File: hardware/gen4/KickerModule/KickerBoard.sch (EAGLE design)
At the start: 110 parts

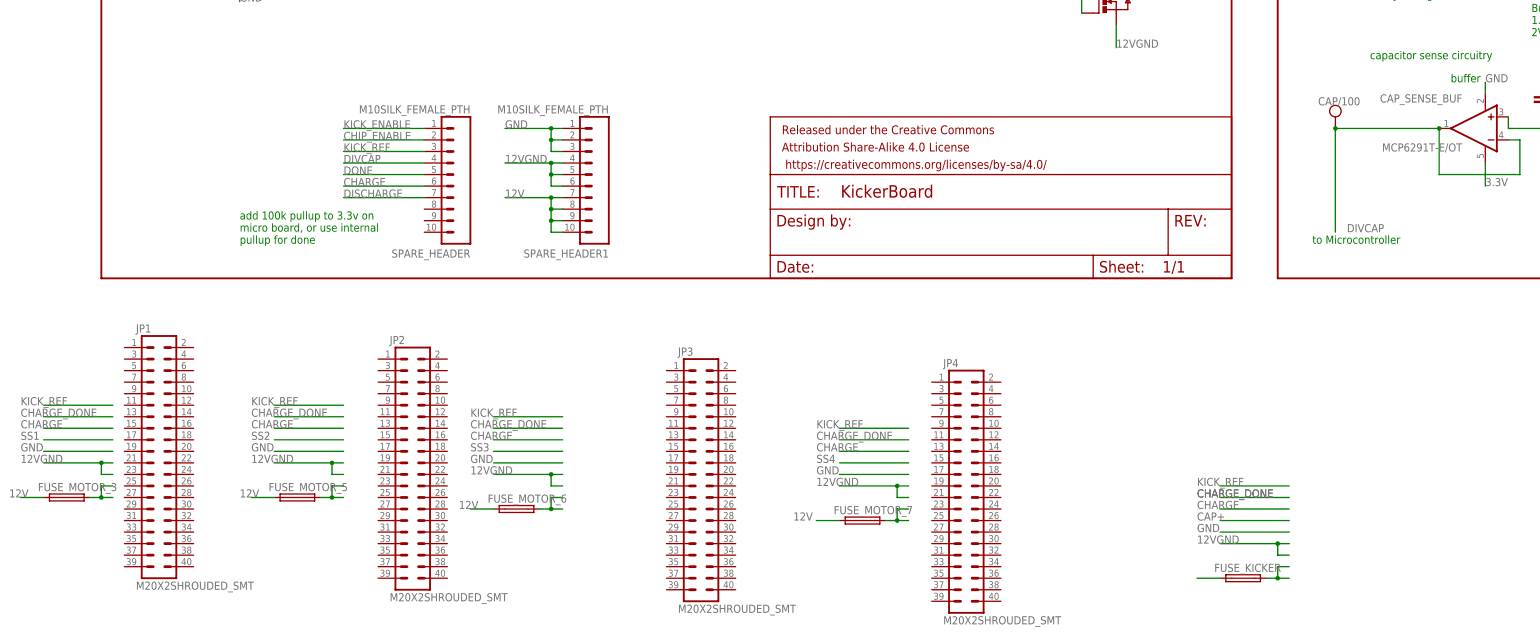
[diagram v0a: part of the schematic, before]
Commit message: Added test points
Placed test point + overlap errors
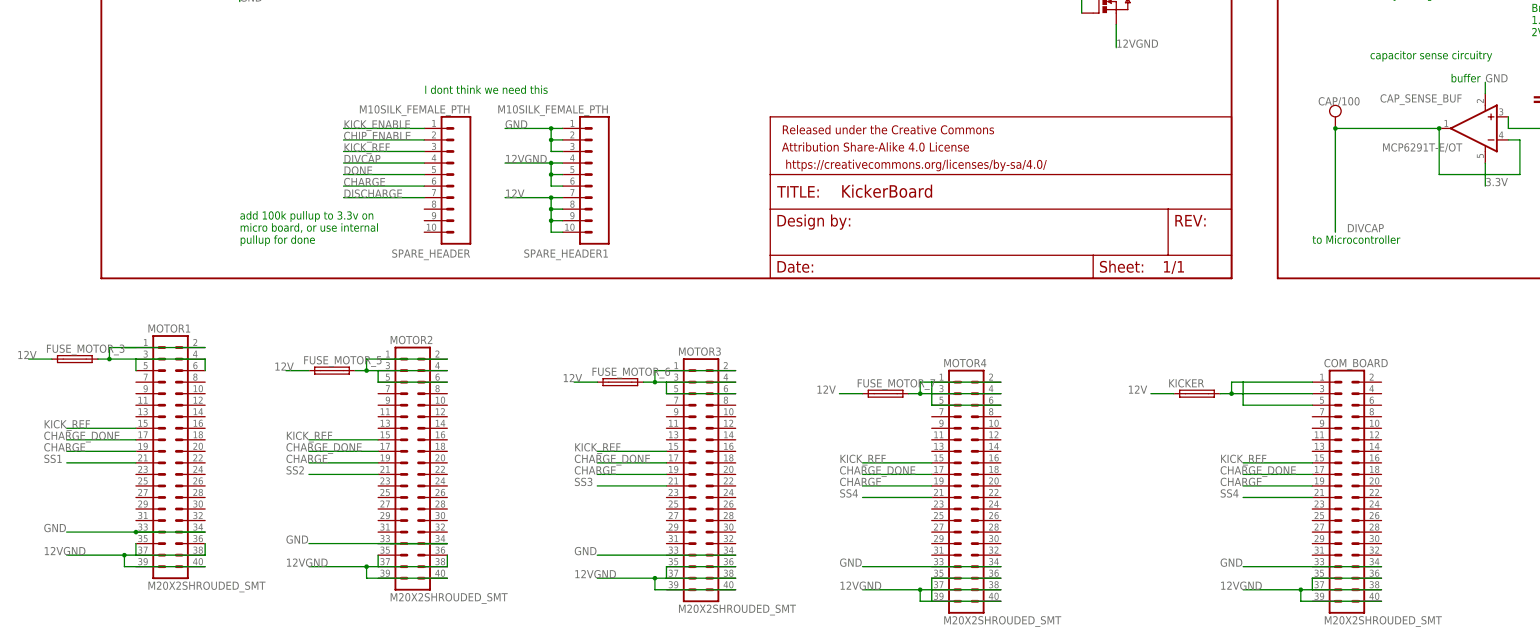
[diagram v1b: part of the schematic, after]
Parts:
- removed FUSE_KICKER: (no value), fuse:TR5
- removed JP1: M20X2SHROUDED_SMT, SparkFun-Connectors:M20X2SHROUDED_SMT
- added COM_BOARD, MOTOR1: M20X2SHROUDED_SMT, SparkFun-Connectors:M20X2SHROUDED_SMT
- added KICKER: (no value), fuse:TR5
- renumbered JP2 to MOTOR2, JP3 to MOTOR3, JP4 to MOTOR4
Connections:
- removed net 12V1: FUSE_KICKER.1
- net 12V: now also KICKER.1
- net 12VGND: now also COM_BOARD.35, COM_BOARD.36, COM_BOARD.38, COM_BOARD.40, MOTOR1.35, MOTOR1.36, MOTOR1.38, MOTOR1.40, MOTOR2.35, MOTOR2.36, MOTOR2.38, MOTOR2.40, MOTOR3.35, MOTOR3.36, MOTOR3.38, MOTOR3.40, MOTOR4.35, MOTOR4.36, MOTOR4.37, MOTOR4.38, MOTOR4.40
- net GND: now also COM_BOARD.34, MOTOR1.33, MOTOR1.34, MOTOR2.34, MOTOR3.34, MOTOR4.34
- net N$25: now also MOTOR4.1, MOTOR4.2, MOTOR4.3, MOTOR4.4, MOTOR4.5, MOTOR4.6
- net N$26: now also MOTOR2.2, MOTOR2.4, MOTOR2.5, MOTOR2.6
- net N$27: now also MOTOR1.1, MOTOR1.2, MOTOR1.4, MOTOR1.5, MOTOR1.6
- net N$28: now also KICKER.2; no longer FUSE_KICKER.2
- net N$4: now also MOTOR3.2, MOTOR3.4, MOTOR3.5, MOTOR3.6
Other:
- note added: "I dont think we need this"
- moved on the sheet: FUSE_MOTOR_3, FUSE_MOTOR_5, FUSE_MOTOR_6, FUSE_MOTOR_7

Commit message: Add SPI pins to board headers and rename old "done" pins.
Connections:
- new net CHARGE_DONE: CHARGE_U.~DN, DONE_LED.A, DONE_TEST.P$1
- new net MISO: MOTOR2.27, MOTOR4.27
- new net MOSI: MOTOR4.25
- new net SCK: MOTOR1.23, MOTOR4.23
- new net SS1: COM_BOARD.20
- new net SS3: COM_BOARD.24
- new net SS4: COM_BOARD.26
- net DONE: no longer CHARGE_U.~DN, DONE_LED.A, DONE_TEST.P$1
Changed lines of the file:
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@@
 <net name="DONE" class="0">
-<segment>
-<wire x1="637.54" y1="304.8" x2="617.22" y2="304.8" width="0.1524" layer="91"/>
-<label x="607.06" y="304.8" size="1.778" layer="95"/>
-<pinref part="CHARGE_U" gate="G$1" pin="~DN"/>
-<pinref part="DONE_TEST" gate="G$1" pin="P$1"/>
-<wire x1="617.22" y1="304.8" x2="607.06" y2="304.8" width="0.1524" layer="91"/>
-<wire x1="617.22" y1="317.5" x2="617.22" y2="304.8" width="0.1524" layer="91"/>
-<junction x="617.22" y="304.8"/>
-</segment>
 <segment>
 <pinref part="SPARE_HEADER" gate="G$1" pin="5"/>
 <wire x1="330.2" y1="215.9" x2="312.42" y2="215.9" width="0.1524" layer="91"/>
 <label x="312.42" y="215.9" size="1.778" layer="95"/>
-</segment>
-<segment>
-<pinref part="DONE_LED" gate="G$1" pin="A"/>
-<wire x1="553.72" y1="358.14" x2="541.02" y2="358.14" width="0.1524" layer="91"/>
-<label x="541.02" y="358.14" size="1.778" layer="95"/>
 </segment>
 </net>
@@
 <wire x1="525.78" y1="149.86" x2="510.54" y2="149.86" width="0.1524" layer="91"/>
 </segment>
+<segment>
+<pinref part="DONE_LED" gate="G$1" pin="A"/>
+<wire x1="553.72" y1="358.14" x2="541.02" y2="358.14" width="0.1524" layer="91"/>
+<label x="541.02" y="358.14" size="1.778" layer="95"/>
+</segment>
+<segment>
+<wire x1="637.54" y1="304.8" x2="617.22" y2="304.8" width="0.1524" layer="91"/>
+<label x="607.06" y="304.8" size="1.778" layer="95"/>
+<pinref part="CHARGE_U" gate="G$1" pin="~DN"/>
+<pinref part="DONE_TEST" gate="G$1" pin="P$1"/>
+<wire x1="617.22" y1="304.8" x2="607.06" y2="304.8" width="0.1524" layer="91"/>
+<wire x1="617.22" y1="317.5" x2="617.22" y2="304.8" width="0.1524" layer="91"/>
+<junction x="617.22" y="304.8"/>
+</segment>
 </net>
 <net name="SS4" class="0">
@@
 </segment>
 <segment>
-<label x="505.46" y="144.78" size="1.778" layer="95"/>
-<wire x1="525.78" y1="144.78" x2="510.54" y2="144.78" width="0.1524" layer="91"/>
+<pinref part="COM_BOARD" gate="G$1" pin="26"/>
+<wire x1="541.02" y1="139.7" x2="553.72" y2="139.7" width="0.1524" layer="91"/>
+<label x="553.72" y="139.7" size="1.778" layer="95"/>
 </segment>
 </net>
@@
 <wire x1="266.7" y1="152.4" x2="251.46" y2="152.4" width="0.1524" layer="91"/>
 </segment>
+<segment>
+<pinref part="COM_BOARD" gate="G$1" pin="20"/>
+<wire x1="541.02" y1="147.32" x2="553.72" y2="147.32" width="0.1524" layer="91"/>
+<label x="553.72" y="147.32" size="1.778" layer="95"/>
+</segment>
 </net>
 <net name="SS2" class="0">
@@
 <wire x1="320.04" y1="149.86" x2="304.8" y2="149.86" width="0.1524" layer="91"/>
 </segment>
+<segment>
+<wire x1="538.48" y1="144.78" x2="553.72" y2="144.78" width="0.1524" layer="91"/>
+<label x="553.72" y="144.78" size="1.778" layer="95"/>
+</segment>
 </net>
 <net name="SS3" class="0">
@@
 <label x="363.22" y="147.32" size="1.778" layer="95"/>
 <wire x1="383.54" y1="147.32" x2="368.3" y2="147.32" width="0.1524" layer="91"/>
+</segment>
+<segment>
+<pinref part="COM_BOARD" gate="G$1" pin="24"/>
+<wire x1="541.02" y1="142.24" x2="553.72" y2="142.24" width="0.1524" layer="91"/>
+<label x="553.72" y="142.24" size="1.778" layer="95"/>
 </segment>
 </net>
@@
 </segment>
 </net>
+<net name="SCK" class="0">
+<segment>
+<wire x1="538.48" y1="137.16" x2="553.72" y2="137.16" width="0.1524" layer="91"/>
+<label x="553.72" y="137.16" size="1.778" layer="95"/>
+</segment>
+<segment>
+<pinref part="MOTOR4" gate="G$1" pin="23"/>
+<wire x1="441.96" y1="142.24" x2="426.72" y2="142.24" width="0.1524" layer="91"/>
+<label x="421.64" y="142.24" size="1.778" layer="95"/>
+</segment>
+<segment>
+<wire x1="386.08" y1="144.78" x2="368.3" y2="144.78" width="0.1524" layer="91"/>
+<label x="363.22" y="144.78" size="1.778" layer="95"/>
+</segment>
+<segment>
+<wire x1="322.58" y1="147.32" x2="304.8" y2="147.32" width="0.1524" layer="91"/>
+<label x="299.72" y="147.32" size="1.778" layer="95"/>
+</segment>
+<segment>
+<pinref part="MOTOR1" gate="G$1" pin="23"/>
+<wire x1="266.7" y1="149.86" x2="251.46" y2="149.86" width="0.1524" layer="91"/>
+<label x="246.38" y="149.86" size="1.778" layer="95"/>
+</segment>
+</net>
+<net name="MOSI" class="0">
+<segment>
+<wire x1="538.48" y1="134.62" x2="553.72" y2="134.62" width="0.1524" layer="91"/>
+<label x="553.72" y="134.62" size="1.778" layer="95"/>
+</segment>
+<segment>
+<pinref part="MOTOR4" gate="G$1" pin="25"/>
+<wire x1="441.96" y1="139.7" x2="426.72" y2="139.7" width="0.1524" layer="91"/>
+<label x="421.64" y="139.7" size="1.778" layer="95"/>
+</segment>
+<segment>
+<wire x1="386.08" y1="142.24" x2="368.3" y2="142.24" width="0.1524" layer="91"/>
+<label x="363.22" y="142.24" size="1.778" layer="95"/>
+</segment>
+<segment>
+<wire x1="322.58" y1="144.78" x2="304.8" y2="144.78" width="0.1524" layer="91"/>
+<label x="299.72" y="144.78" size="1.778" layer="95"/>
+</segment>
+<segment>
+<wire x1="269.24" y1="147.32" x2="251.46" y2="147.32" width="0.1524" layer="91"/>
+<label x="246.38" y="147.32" size="1.778" layer="95"/>
+</segment>
+</net>
+<net name="MISO" class="0">
+<segment>
+<wire x1="538.48" y1="132.08" x2="553.72" y2="132.08" width="0.1524" layer="91"/>
+<label x="553.72" y="132.08" size="1.778" layer="95"/>
+</segment>
+<segment>
+<pinref part="MOTOR4" gate="G$1" pin="27"/>
+<wire x1="441.96" y1="137.16" x2="426.72" y2="137.16" width="0.1524" layer="91"/>
+<label x="421.64" y="137.16" size="1.778" layer="95"/>
+</segment>
+<segment>
+<wire x1="386.08" y1="139.7" x2="368.3" y2="139.7" width="0.1524" layer="91"/>
+<label x="363.22" y="139.7" size="1.778" layer="95"/>
+</segment>
+<segment>
+<pinref part="MOTOR2" gate="G$1" pin="27"/>
+<wire x1="320.04" y1="142.24" x2="304.8" y2="142.24" width="0.1524" layer="91"/>
+<label x="299.72" y="142.24" size="1.778" layer="95"/>
+</segment>
+<segment>
+<wire x1="269.24" y1="144.78" x2="251.46" y2="144.78" width="0.1524" layer="91"/>
+<label x="246.38" y="144.78" size="1.778" layer="95"/>
+</segment>
+</net>

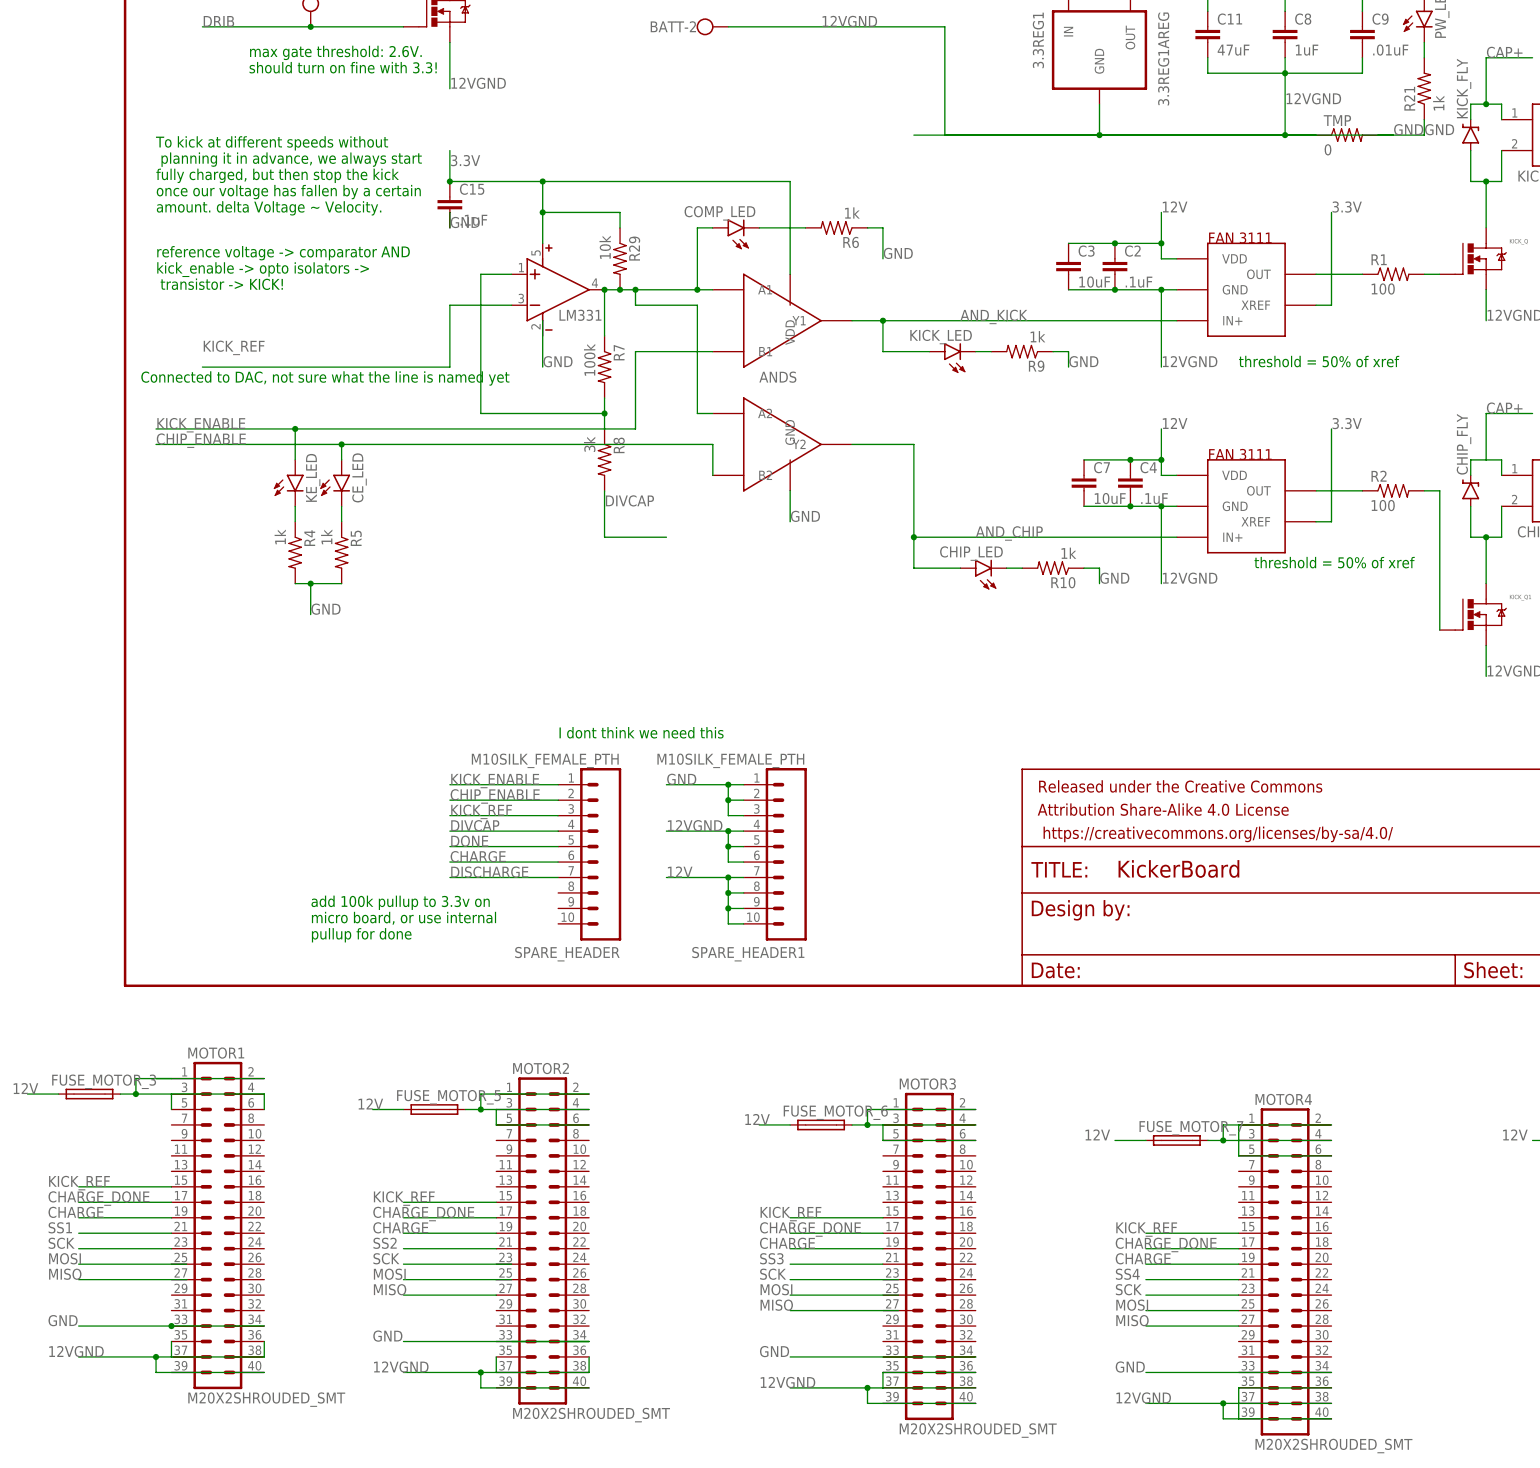
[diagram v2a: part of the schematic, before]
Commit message: layout on mainboard
layout on mainboard almost done.
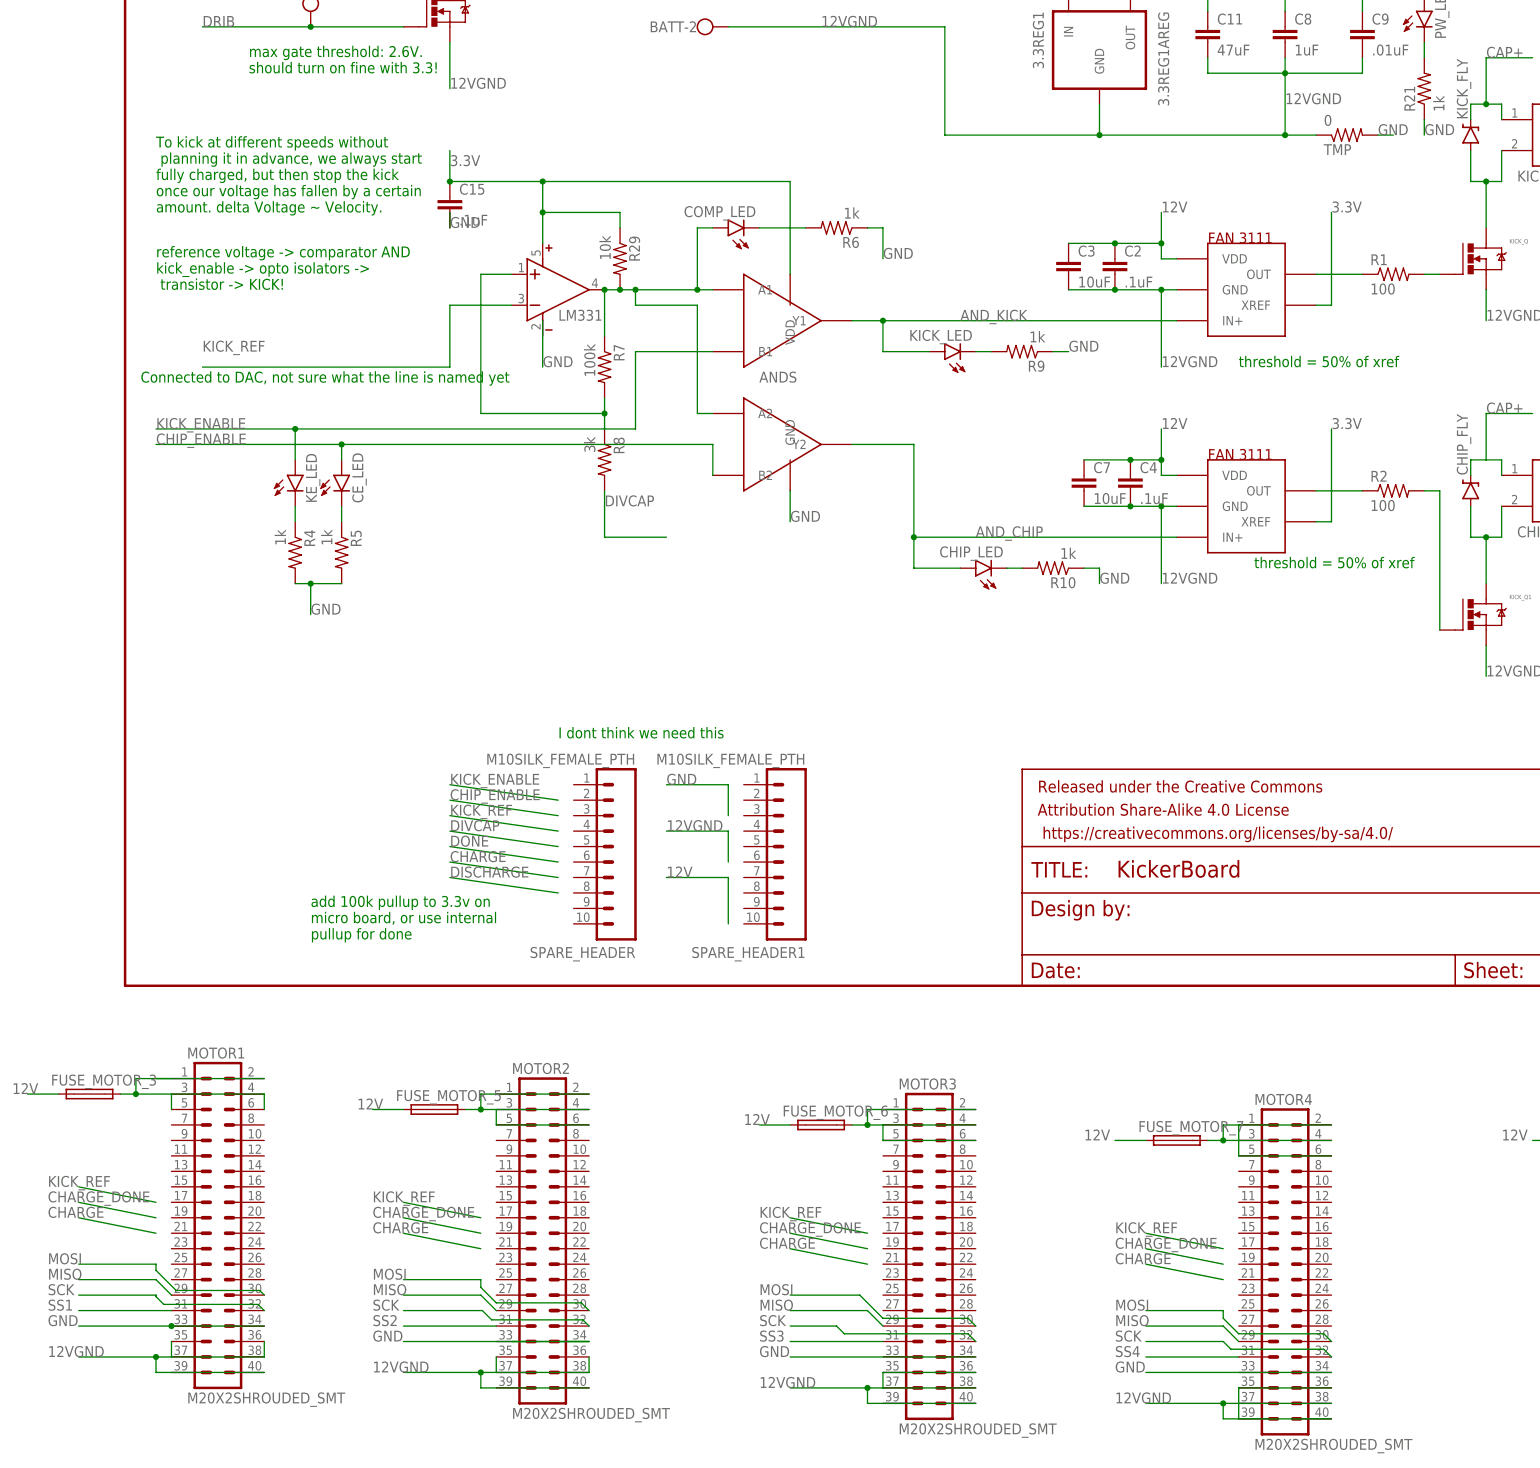
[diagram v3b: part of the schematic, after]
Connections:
- removed net DONE: SPARE_HEADER.5
- new net SS2: MOTOR2.31
- net 12V: no longer SPARE_HEADER1.10, SPARE_HEADER1.7, SPARE_HEADER1.8, SPARE_HEADER1.9
- net 12VGND: no longer SPARE_HEADER1.4, SPARE_HEADER1.5, SPARE_HEADER1.6
- net CHARGE: no longer SPARE_HEADER.6
- net CHIP_ENABLE: no longer SPARE_HEADER.2
- net DISCHARGE: no longer SPARE_HEADER.7
- net DIVCAP: no longer SPARE_HEADER.4
- net GND: no longer SPARE_HEADER1.1, SPARE_HEADER1.2, SPARE_HEADER1.3
- net KICK_ENABLE: no longer SPARE_HEADER.1
- net KICK_REF: no longer SPARE_HEADER.3
- net MISO: now also MOTOR1.29, MOTOR2.29, MOTOR3.29, MOTOR4.29; no longer MOTOR2.27, MOTOR4.27
- net MOSI: now also MOTOR1.30, MOTOR2.30, MOTOR3.30, MOTOR4.30; no longer MOTOR4.25
- net SCK: now also MOTOR1.32, MOTOR2.32, MOTOR3.32, MOTOR4.32; no longer MOTOR1.23, MOTOR4.23
- net SS1: now also MOTOR1.31
- net SS3: now also MOTOR3.31
- net SS4: now also MOTOR4.31
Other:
- moved on the sheet: SPARE_HEADER, TMP

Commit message: Mainboard progress
connecting up stuff
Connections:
- removed net N$16: 12V_TEST.P$1, 3.3REG1.IN, ON/OFF.P2
- net 12V: now also 12V_TEST.P$1, 3.3REG1.IN, ON/OFF.P2
- net 12VGND: now also COM_BOARD.37, COM_BOARD.39, MOTOR1.37, MOTOR1.39, MOTOR2.37, MOTOR2.39, MOTOR3.37, MOTOR3.39, MOTOR4.39
- net GND: now also COM_BOARD.33, MOTOR2.33, MOTOR3.33, MOTOR4.33
- net MISO: now also COM_BOARD.32
- net MOSI: now also COM_BOARD.30
- net SCK: now also COM_BOARD.28
- net SS2: now also COM_BOARD.22
